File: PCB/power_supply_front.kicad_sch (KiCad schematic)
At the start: 41 parts, among them IC1 LM66200, IC2 ESDALC6V1W5, J1 Screw_Terminal_01x04, J2 VBUS/GND for the stacked PCB, J3 1935789, J4 VBUS/GND for the stacked PCB, J5 Power Supply, J6 Screw_Terminal_01x04, U10 H11L1, U6 TS3USB30EDGSR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

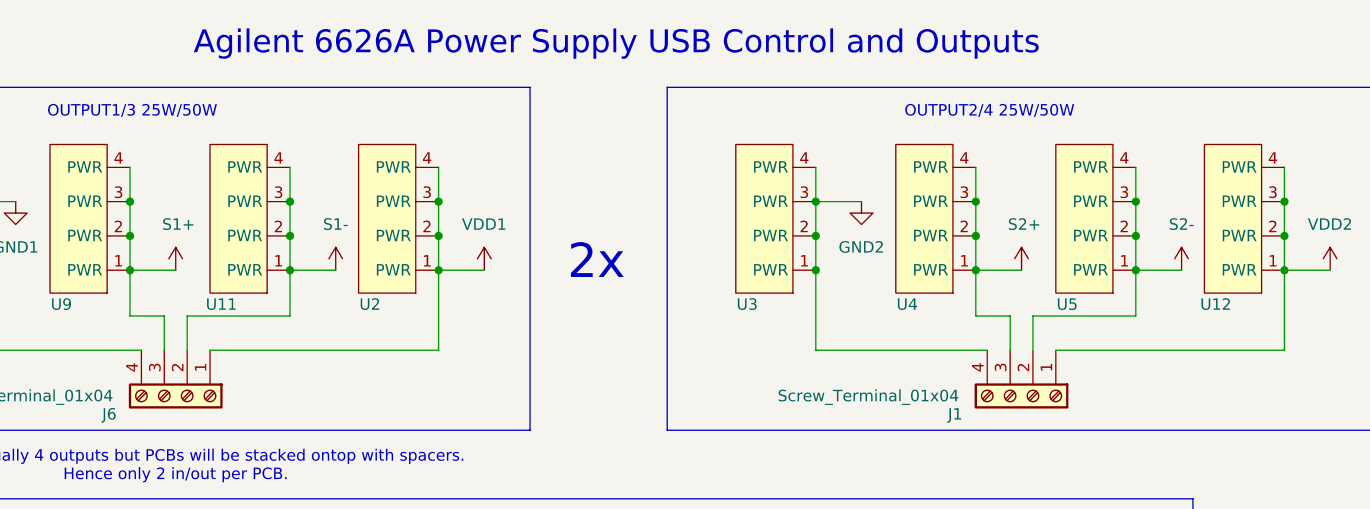
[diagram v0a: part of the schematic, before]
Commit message: Adjust plug spacing. Add label connector pinout on silkscreen.
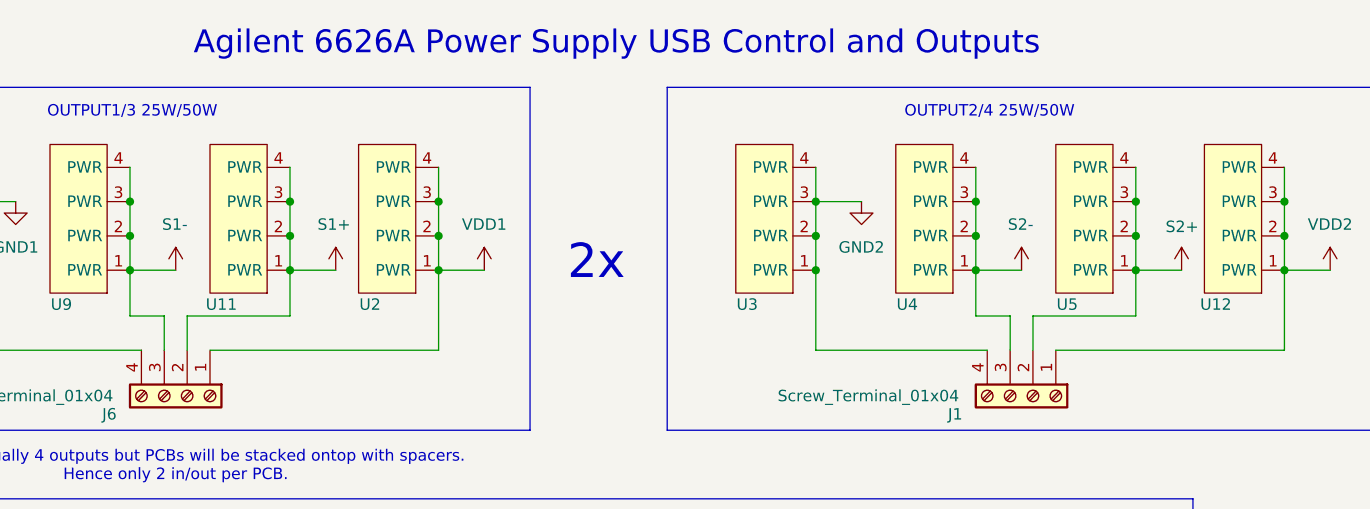
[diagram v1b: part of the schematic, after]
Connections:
- net S1+: now also J6.2 (Pin_2), U11.1 (PWR), U11.2 (PWR), U11.3 (PWR), U11.4 (PWR); no longer J6.3 (Pin_3), U9.1 (PWR), U9.2 (PWR), U9.3 (PWR), U9.4 (PWR)
- net S1-: now also J6.3 (Pin_3), U9.1 (PWR), U9.2 (PWR), U9.3 (PWR), U9.4 (PWR); no longer J6.2 (Pin_2), U11.1 (PWR), U11.2 (PWR), U11.3 (PWR), U11.4 (PWR)
- net S2+: now also J1.2 (Pin_2), U5.1 (PWR), U5.2 (PWR), U5.3 (PWR), U5.4 (PWR); no longer J1.3 (Pin_3), U4.1 (PWR), U4.2 (PWR), U4.3 (PWR), U4.4 (PWR)
- net S2-: now also J1.3 (Pin_3), U4.1 (PWR), U4.2 (PWR), U4.3 (PWR), U4.4 (PWR); no longer J1.2 (Pin_2), U5.1 (PWR), U5.2 (PWR), U5.3 (PWR), U5.4 (PWR)
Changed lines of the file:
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@@
 		(on_board yes)
 		(dnp no)
-		(fields_autoplaced yes)
 		(property "Reference" "#PWR05"
 			(at 170.18 45.72 0)
@@
 			)
 		)
-		(property "Value" "S2-"
-			(at 170.18 36.83 0)
+		(property "Value" "S2+"
+			(at 168.402 37.084 0)
 			(effects
 				(font
 					(size 1.27 1.27)
 				)
+				(justify left)
 			)
 		)
@@
 			)
 		)
-		(property "Value" "S2+"
+		(property "Value" "S2-"
 			(at 150.876 36.83 0)
 			(effects
@@
 		(on_board yes)
 		(dnp no)
-		(fields_autoplaced yes)
 		(property "Reference" "#PWR038"
 			(at 76.2 45.72 0)
@@
 			)
 		)
-		(property "Value" "S1-"
-			(at 76.2 36.83 0)
+		(property "Value" "S1+"
+			(at 74.168 36.83 0)
 			(effects
 				(font
 					(size 1.27 1.27)
 				)
+				(justify left)
 			)
 		)
@@
 			)
 		)
-		(property "Value" "S1+"
+		(property "Value" "S1-"
 			(at 56.896 36.83 0)
 			(effects
